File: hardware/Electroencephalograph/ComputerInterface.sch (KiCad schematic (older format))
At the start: 14 parts, among them J5 USB_B_Micro, U6 FT200XD

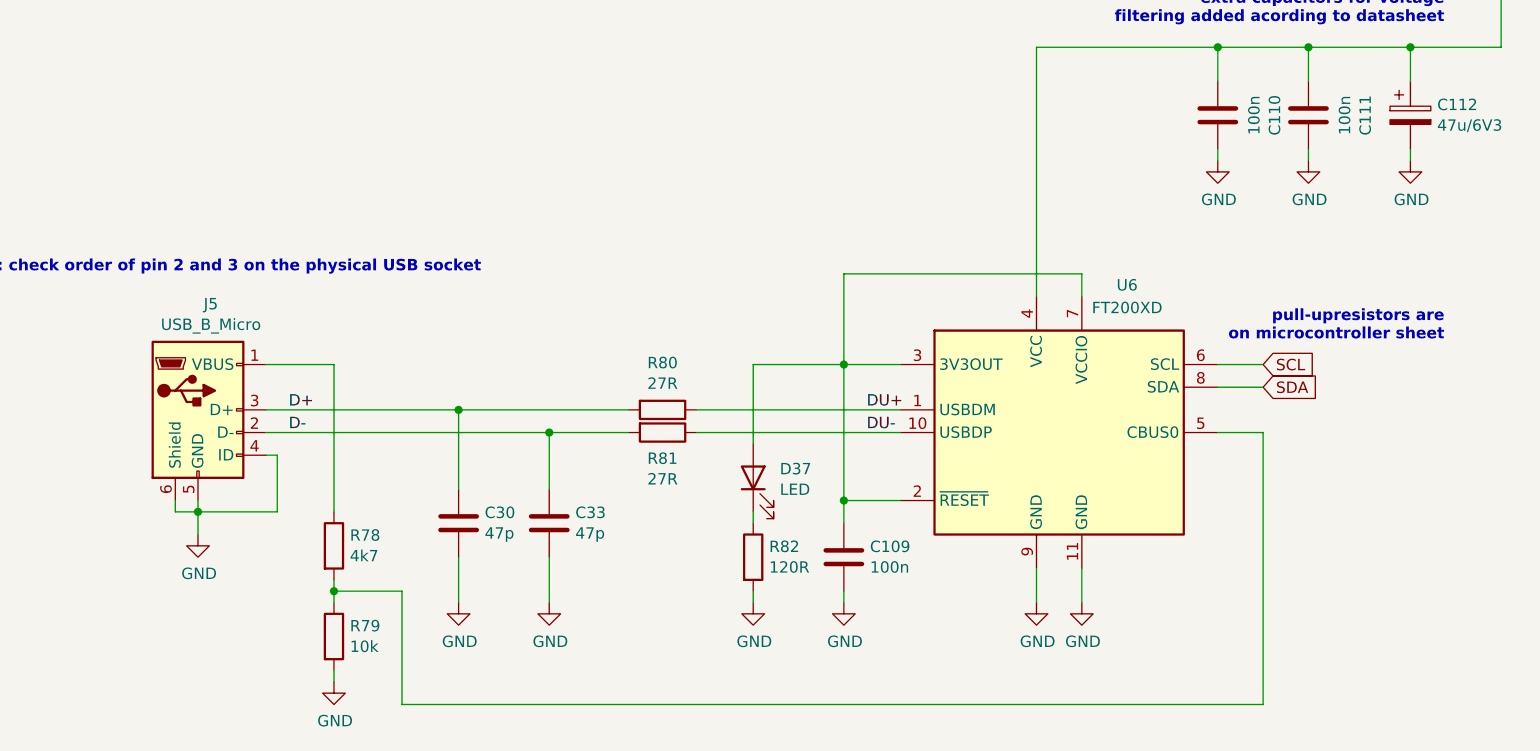
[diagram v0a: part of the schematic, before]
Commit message: placement of usb interface, fix in grounds
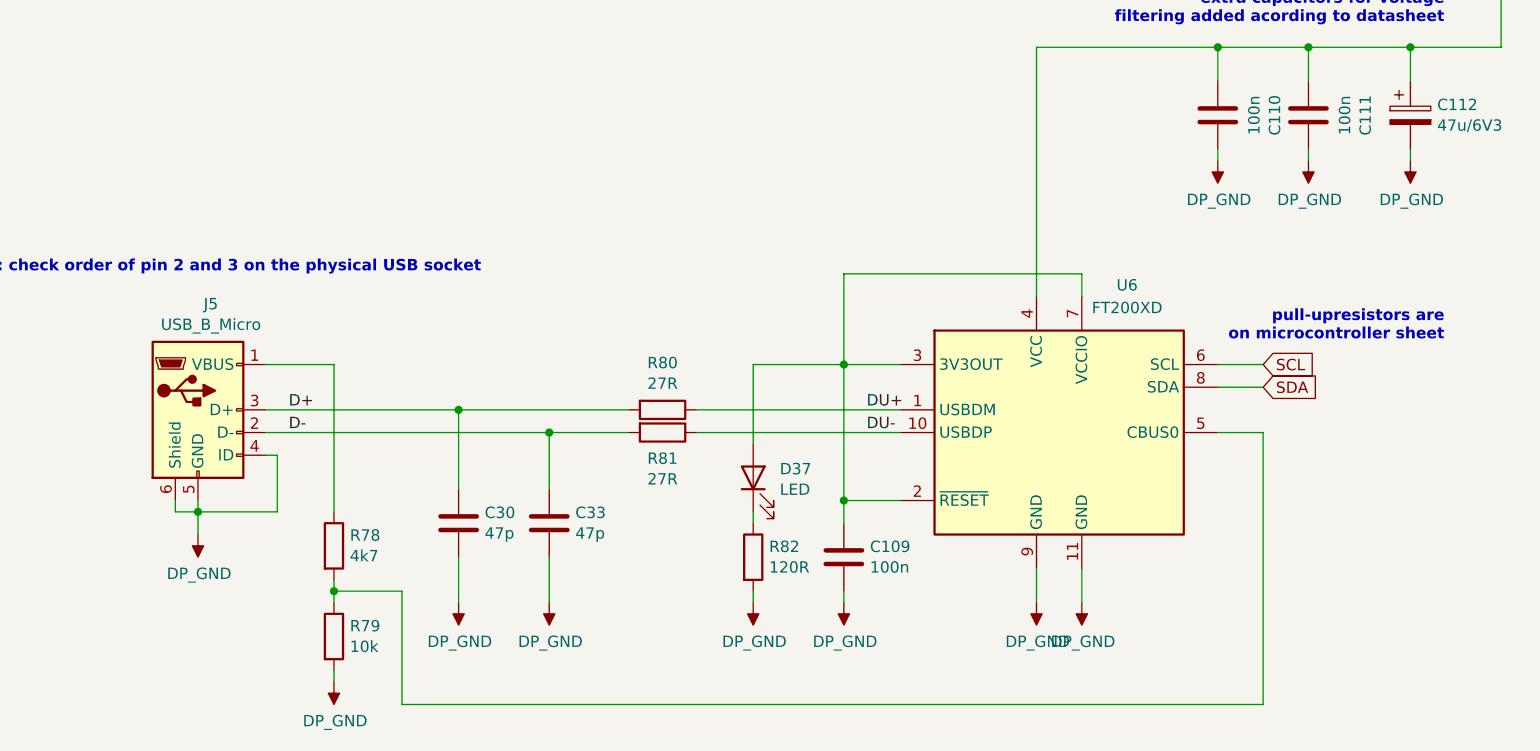
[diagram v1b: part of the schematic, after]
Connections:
- net GND renamed DP_GND
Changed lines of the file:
@@
 encoding utf-8
 Sheet 8 8
-Title ""
+Title "Computer interface"
 Date ""
-Rev ""
-Comp ""
+Rev "1.0"
+Comp "MIT License"
 Comment1 ""
 Comment2 ""
@@
 $EndComp
 $Comp
-L power:GND #PWR?
+L Electroencephalograph:DP_GND #PWR?
 U 1 1 5DDD73E7
 P 3250 4350
@@
 AR Path="/5E27E78E/5DDD73E7" Ref="#PWR057"  Part="1"
 F 0 "#PWR057" H 3250 4100 50  0001 C CNN
-F 1 "GND" H 3255 4177 50  0000 C CNN
+F 1 "DP_GND" H 3255 4177 50  0000 C CNN
 F 2 "" H 3250 4350 50  0001 C CNN
 F 3 "" H 3250 4350 50  0001 C CNN
@@
 	5700 4250 5700 4300
 $Comp
-L power:GND #PWR?
+L Electroencephalograph:DP_GND #PWR?
 U 1 1 5DDD73F8
 P 5700 4650
@@
 AR Path="/5E27E78E/5DDD73F8" Ref="#PWR0197"  Part="1"
 F 0 "#PWR0197" H 5700 4400 50  0001 C CNN
-F 1 "GND" H 5705 4477 50  0000 C CNN
+F 1 "DP_GND" H 5705 4477 50  0000 C CNN
 F 2 "" H 5700 4650 50  0001 C CNN
 F 3 "" H 5700 4650 50  0001 C CNN
@@
 	5700 4650 5700 4600
 $Comp
-L power:GND #PWR?
+L Electroencephalograph:DP_GND #PWR?
 U 1 1 5DD1D08B
 P 6950 4650
@@
 AR Path="/5E27E78E/5DD1D08B" Ref="#PWR0199"  Part="1"
 F 0 "#PWR0199" H 6950 4400 50  0001 C CNN
-F 1 "GND" H 6955 4477 50  0000 C CNN
+F 1 "DP_GND" H 6955 4477 50  0000 C CNN
 F 2 "" H 6950 4650 50  0001 C CNN
 F 3 "" H 6950 4650 50  0001 C CNN
@@
 $EndComp
 $Comp
-L power:GND #PWR?
+L Electroencephalograph:DP_GND #PWR?
 U 1 1 5DD1D475
 P 7150 4650
@@
 AR Path="/5E27E78E/5DD1D475" Ref="#PWR0200"  Part="1"
 F 0 "#PWR0200" H 7150 4400 50  0001 C CNN
-F 1 "GND" H 7155 4477 50  0000 C CNN
+F 1 "DP_GND" H 7155 4477 50  0000 C CNN
 F 2 "" H 7150 4650 50  0001 C CNN
 F 3 "" H 7150 4650 50  0001 C CNN
@@
 	4400 3800 4400 4150
 $Comp
-L power:GND #PWR?
+L Electroencephalograph:DP_GND #PWR?
 U 1 1 5DD256FC
 P 4400 4650
@@
 AR Path="/5E27E78E/5DD256FC" Ref="#PWR064"  Part="1"
 F 0 "#PWR064" H 4400 4400 50  0001 C CNN
-F 1 "GND" H 4405 4477 50  0000 C CNN
+F 1 "DP_GND" H 4405 4477 50  0000 C CNN
 F 2 "" H 4400 4650 50  0001 C CNN
 F 3 "" H 4400 4650 50  0001 C CNN
@@
 $EndComp
 $Comp
-L power:GND #PWR?
+L Electroencephalograph:DP_GND #PWR?
 U 1 1 5DD25C76
 P 4800 4650
@@
 AR Path="/5E27E78E/5DD25C76" Ref="#PWR0196"  Part="1"
 F 0 "#PWR0196" H 4800 4400 50  0001 C CNN
-F 1 "GND" H 4805 4477 50  0000 C CNN
+F 1 "DP_GND" H 4805 4477 50  0000 C CNN
 F 2 "" H 4800 4650 50  0001 C CNN
 F 3 "" H 4800 4650 50  0001 C CNN
@@
 $EndComp
 $Comp
-L power:GND #PWR?
+L Electroencephalograph:DP_GND #PWR?
 U 1 1 5DD2774B
 P 6100 4650
@@
 AR Path="/5E27E78E/5DD2774B" Ref="#PWR0198"  Part="1"
 F 0 "#PWR0198" H 6100 4400 50  0001 C CNN
-F 1 "GND" H 6105 4477 50  0000 C CNN
+F 1 "DP_GND" H 6105 4477 50  0000 C CNN
 F 2 "" H 6100 4650 50  0001 C CNN
 F 3 "" H 6100 4650 50  0001 C CNN
@@
 	3850 3600 3850 4250
 $Comp
-L power:GND #PWR?
+L Electroencephalograph:DP_GND #PWR?
 U 1 1 5DD46299
 P 3850 5000
@@
 AR Path="/5E27E78E/5DD46299" Ref="#PWR058"  Part="1"
 F 0 "#PWR058" H 3850 4750 50  0001 C CNN
-F 1 "GND" H 3855 4827 50  0000 C CNN
+F 1 "DP_GND" H 3855 4827 50  0000 C CNN
 F 2 "" H 3850 5000 50  0001 C CNN
 F 3 "" H 3850 5000 50  0001 C CNN
@@
 $EndComp
 $Comp
-L power:GND #PWR?
+L Electroencephalograph:DP_GND #PWR?
 U 1 1 5DE7AD55
 P 8600 2700
@@
 AR Path="/5E27E78E/5DE7AD55" Ref="#PWR0203"  Part="1"
 F 0 "#PWR0203" H 8600 2450 50  0001 C CNN
-F 1 "GND" H 8605 2527 50  0000 C CNN
+F 1 "DP_GND" H 8605 2527 50  0000 C CNN
 F 2 "" H 8600 2700 50  0001 C CNN
 F 3 "" H 8600 2700 50  0001 C CNN
@@
 $EndComp
 $Comp
-L power:GND #PWR?
+L Electroencephalograph:DP_GND #PWR?
 U 1 1 5DE8245F
 P 8150 2700
@@
 AR Path="/5E27E78E/5DE8245F" Ref="#PWR0202"  Part="1"
 F 0 "#PWR0202" H 8150 2450 50  0001 C CNN
-F 1 "GND" H 8155 2527 50  0000 C CNN
+F 1 "DP_GND" H 8155 2527 50  0000 C CNN
 F 2 "" H 8150 2700 50  0001 C CNN
 F 3 "" H 8150 2700 50  0001 C CNN
@@
 $EndComp
 $Comp
-L power:GND #PWR?
+L Electroencephalograph:DP_GND #PWR?
 U 1 1 5DE8272A
 P 7750 2700
@@
 AR Path="/5E27E78E/5DE8272A" Ref="#PWR0201"  Part="1"
 F 0 "#PWR0201" H 7750 2450 50  0001 C CNN
-F 1 "GND" H 7755 2527 50  0000 C CNN
+F 1 "DP_GND" H 7755 2527 50  0000 C CNN
 F 2 "" H 7750 2700 50  0001 C CNN
 F 3 "" H 7750 2700 50  0001 C CNN

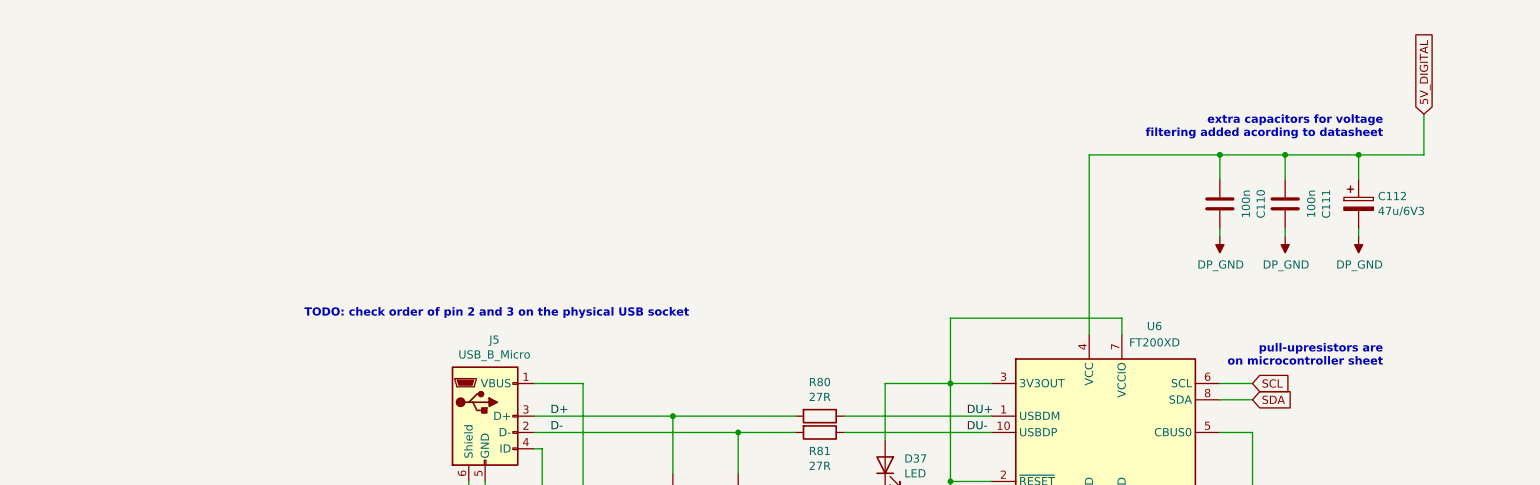
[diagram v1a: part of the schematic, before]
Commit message: fix #41, fix #18
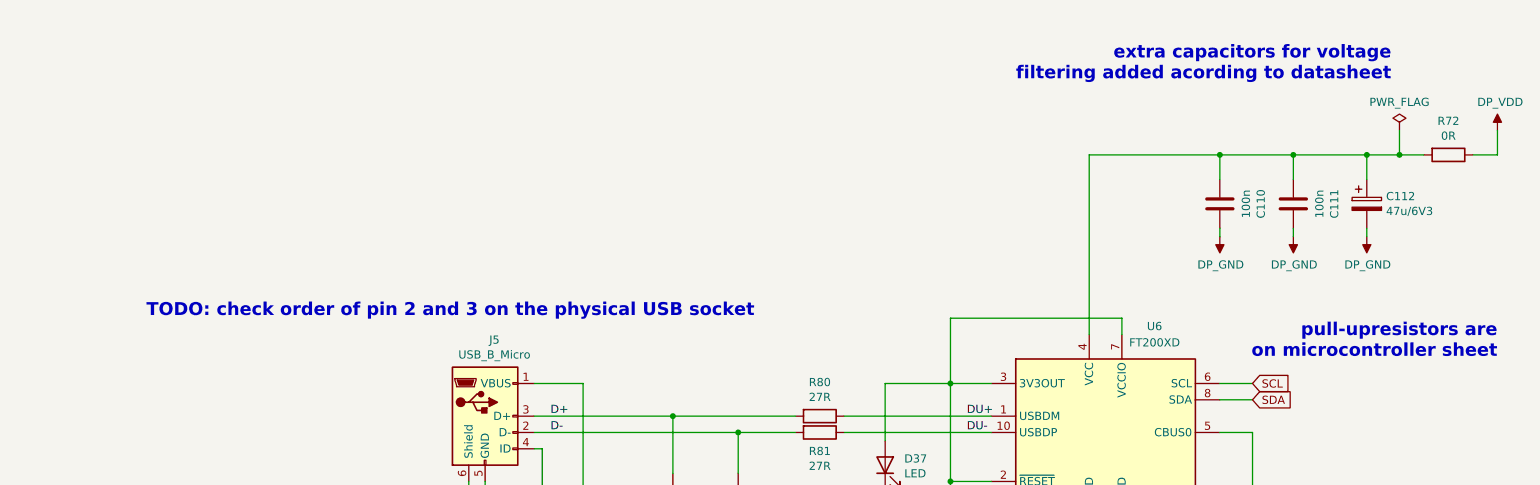
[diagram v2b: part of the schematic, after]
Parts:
- added R72: 0R, Resistor_SMD:R_0402_1005Metric, symbol Device:R
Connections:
- net 5V_DIGITAL: no longer names the net of C110.1, C111.1, C112.1, U6.4 (VCC)
- net 5V_DIGITAL: now also R72.2
- new net DP_VDD: R72.1
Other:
- moved on the sheet: C111, C112
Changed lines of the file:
@@
 $Descr A4 11693 8268
 encoding utf-8
-Sheet 8 8
+Sheet 8 9
 Title "Computer interface"
 Date ""
@@
 AR Path="/5DD5C7F6/5DDD73E7" Ref="#PWR?"  Part="1"
 AR Path="/5DD5CD1D/5DDD73E7" Ref="#PWR?"  Part="1"
-AR Path="/5E27E78E/5DDD73E7" Ref="#PWR057"  Part="1"
-F 0 "#PWR057" H 3250 4100 50  0001 C CNN
+AR Path="/5E27E78E/5DDD73E7" Ref="#PWR57"  Part="1"
+F 0 "#PWR57" H 3250 4100 50  0001 C CNN
 F 1 "DP_GND" H 3255 4177 50  0000 C CNN
 F 2 "" H 3250 4350 50  0001 C CNN
@@
 AR Path="/5DD5C7F6/5DDD73F8" Ref="#PWR?"  Part="1"
 AR Path="/5DD5CD1D/5DDD73F8" Ref="#PWR?"  Part="1"
-AR Path="/5E27E78E/5DDD73F8" Ref="#PWR0197"  Part="1"
-F 0 "#PWR0197" H 5700 4400 50  0001 C CNN
+AR Path="/5E27E78E/5DDD73F8" Ref="#PWR197"  Part="1"
+F 0 "#PWR197" H 5700 4400 50  0001 C CNN
 F 1 "DP_GND" H 5705 4477 50  0000 C CNN
 F 2 "" H 5700 4650 50  0001 C CNN
@@
 AR Path="/5DD5C7F6/5DD1D08B" Ref="#PWR?"  Part="1"
 AR Path="/5DD5CD1D/5DD1D08B" Ref="#PWR?"  Part="1"
-AR Path="/5E27E78E/5DD1D08B" Ref="#PWR0199"  Part="1"
-F 0 "#PWR0199" H 6950 4400 50  0001 C CNN
+AR Path="/5E27E78E/5DD1D08B" Ref="#PWR199"  Part="1"
+F 0 "#PWR199" H 6950 4400 50  0001 C CNN
 F 1 "DP_GND" H 6955 4477 50  0000 C CNN
 F 2 "" H 6950 4650 50  0001 C CNN
@@
 AR Path="/5DD5C7F6/5DD1D475" Ref="#PWR?"  Part="1"
 AR Path="/5DD5CD1D/5DD1D475" Ref="#PWR?"  Part="1"
-AR Path="/5E27E78E/5DD1D475" Ref="#PWR0200"  Part="1"
-F 0 "#PWR0200" H 7150 4400 50  0001 C CNN
+AR Path="/5E27E78E/5DD1D475" Ref="#PWR200"  Part="1"
+F 0 "#PWR200" H 7150 4400 50  0001 C CNN
 F 1 "DP_GND" H 7155 4477 50  0000 C CNN
 F 2 "" H 7150 4650 50  0001 C CNN
@@
 Text GLabel 7950 3700 2    50   Input ~ 0
 SDA
-Text Notes 8750 3500 2    50   ~ 10
+Text Notes 9450 3450 2    79   ~ 16
 pull-upresistors are \non microcontroller sheet
 Wire Wire Line
@@
 AR Path="/5DD5C7F6/5DD256FC" Ref="#PWR?"  Part="1"
 AR Path="/5DD5CD1D/5DD256FC" Ref="#PWR?"  Part="1"
-AR Path="/5E27E78E/5DD256FC" Ref="#PWR064"  Part="1"
-F 0 "#PWR064" H 4400 4400 50  0001 C CNN
+AR Path="/5E27E78E/5DD256FC" Ref="#PWR64"  Part="1"
+F 0 "#PWR64" H 4400 4400 50  0001 C CNN
 F 1 "DP_GND" H 4405 4477 50  0000 C CNN
 F 2 "" H 4400 4650 50  0001 C CNN
@@
 AR Path="/5DD5C7F6/5DD25C76" Ref="#PWR?"  Part="1"
 AR Path="/5DD5CD1D/5DD25C76" Ref="#PWR?"  Part="1"
-AR Path="/5E27E78E/5DD25C76" Ref="#PWR0196"  Part="1"
-F 0 "#PWR0196" H 4800 4400 50  0001 C CNN
+AR Path="/5E27E78E/5DD25C76" Ref="#PWR196"  Part="1"
+F 0 "#PWR196" H 4800 4400 50  0001 C CNN
 F 1 "DP_GND" H 4805 4477 50  0000 C CNN
 F 2 "" H 4800 4650 50  0001 C CNN
@@
 AR Path="/5DD5C7F6/5DD2774B" Ref="#PWR?"  Part="1"
 AR Path="/5DD5CD1D/5DD2774B" Ref="#PWR?"  Part="1"
-AR Path="/5E27E78E/5DD2774B" Ref="#PWR0198"  Part="1"
-F 0 "#PWR0198" H 6100 4400 50  0001 C CNN
+AR Path="/5E27E78E/5DD2774B" Ref="#PWR198"  Part="1"
+F 0 "#PWR198" H 6100 4400 50  0001 C CNN
 F 1 "DP_GND" H 6105 4477 50  0000 C CNN
 F 2 "" H 6100 4650 50  0001 C CNN
@@
 Wire Wire Line
 	3600 4250 3250 4250
-Text Notes 4500 3200 2    50   ~ 10
+Text Notes 4900 3200 2    79   ~ 16
 TODO: check order of pin 2 and 3 on the physical USB socket
 Wire Wire Line
@@
 	6100 3200 6100 3600
 Wire Wire Line
-	9000 1950 9000 2200
+	9450 2050 9450 2200
 $Comp
 L Device:C C?
@@
 AR Path="/5DD5C7F6/5DD46299" Ref="#PWR?"  Part="1"
 AR Path="/5DD5CD1D/5DD46299" Ref="#PWR?"  Part="1"
-AR Path="/5E27E78E/5DD46299" Ref="#PWR058"  Part="1"
-F 0 "#PWR058" H 3850 4750 50  0001 C CNN
+AR Path="/5E27E78E/5DD46299" Ref="#PWR58"  Part="1"
+F 0 "#PWR58" H 3850 4750 50  0001 C CNN
 F 1 "DP_GND" H 3855 4827 50  0000 C CNN
 F 2 "" H 3850 5000 50  0001 C CNN
@@
 Wire Wire Line
 	5450 3800 6350 3800
-Text GLabel 9000 1950 1    50   Input ~ 0
-5V_DIGITAL
 Wire Wire Line
 	6100 3600 5700 3600
@@
 L Device:CP C?
 U 1 1 5DE7AD4F
-P 8600 2500
+P 8650 2500
 AR Path="/5DE7AD4F" Ref="C?"  Part="1"
 AR Path="/5DAEEEF4/5DE7AD4F" Ref="C?"  Part="1"
@@
 AR Path="/5DD5CD1D/5DE7AD4F" Ref="C?"  Part="1"
 AR Path="/5E27E78E/5DE7AD4F" Ref="C112"  Part="1"
-F 0 "C112" H 8718 2546 50  0000 L CNN
-F 1 "47u/6V3" H 8718 2455 50  0000 L CNN
-F 2 "Capacitor_Tantalum_SMD:CP_EIA-3528-21_Kemet-B" H 8638 2350 50  0001 C CNN
-F 3 "~" H 8600 2500 50  0001 C CNN
-	1    8600 2500
+F 0 "C112" H 8768 2546 50  0000 L CNN
+F 1 "47u/6V3" H 8768 2455 50  0000 L CNN
+F 2 "Capacitor_Tantalum_SMD:CP_EIA-3528-21_Kemet-B" H 8688 2350 50  0001 C CNN
+F 3 "~" H 8650 2500 50  0001 C CNN
+	1    8650 2500
 	1    0    0    -1
 $EndComp
@@
 L Electroencephalograph:DP_GND #PWR?
 U 1 1 5DE7AD55
-P 8600 2700
+P 8650 2700
 AR Path="/5DE7AD55" Ref="#PWR?"  Part="1"
 AR Path="/5DAEEEF4/5DE7AD55" Ref="#PWR?"  Part="1"
 AR Path="/5DD5C7F6/5DE7AD55" Ref="#PWR?"  Part="1"
 AR Path="/5DD5CD1D/5DE7AD55" Ref="#PWR?"  Part="1"
-AR Path="/5E27E78E/5DE7AD55" Ref="#PWR0203"  Part="1"
-F 0 "#PWR0203" H 8600 2450 50  0001 C CNN
-F 1 "DP_GND" H 8605 2527 50  0000 C CNN
-F 2 "" H 8600 2700 50  0001 C CNN
-F 3 "" H 8600 2700 50  0001 C CNN
-	1    8600 2700
-	1    0    0    -1
-$EndComp
-Wire Wire Line
-	8600 2700 8600 2650
+AR Path="/5E27E78E/5DE7AD55" Ref="#PWR203"  Part="1"
+F 0 "#PWR203" H 8650 2450 50  0001 C CNN
+F 1 "DP_GND" H 8655 2527 50  0000 C CNN
+F 2 "" H 8650 2700 50  0001 C CNN
+F 3 "" H 8650 2700 50  0001 C CNN
+	1    8650 2700
+	1    0    0    -1
+$EndComp
+Wire Wire Line
+	8650 2700 8650 2650
 $Comp
 L Device:C C?
 U 1 1 5DE7B775
-P 8150 2500
+P 8200 2500
 AR Path="/5DE7B775" Ref="C?"  Part="1"
 AR Path="/5DAEEEF4/5DE7B775" Ref="C?"  Part="1"
@@
 AR Path="/5DD5CD1D/5DE7B775" Ref="C?"  Part="1"
 AR Path="/5E27E78E/5DE7B775" Ref="C111"  Part="1"
-F 0 "C111" V 8402 2500 50  0000 C CNN
-F 1 "100n" V 8311 2500 50  0000 C CNN
-F 2 "Capacitor_SMD:C_0402_1005Metric" H 8188 2350 50  0001 C CNN
-F 3 "~" H 8150 2500 50  0001 C CNN
-	1    8150 2500
+F 0 "C111" V 8452 2500 50  0000 C CNN
+F 1 "100n" V 8361 2500 50  0000 C CNN
+F 2 "Capacitor_SMD:C_0402_1005Metric" H 8238 2350 50  0001 C CNN
+F 3 "~" H 8200 2500 50  0001 C CNN
+	1    8200 2500
 	1    0    0    -1
 $EndComp
@@
 L Electroencephalograph:DP_GND #PWR?
 U 1 1 5DE8245F
-P 8150 2700
+P 8200 2700
 AR Path="/5DE8245F" Ref="#PWR?"  Part="1"
 AR Path="/5DAEEEF4/5DE8245F" Ref="#PWR?"  Part="1"
 AR Path="/5DD5C7F6/5DE8245F" Ref="#PWR?"  Part="1"
 AR Path="/5DD5CD1D/5DE8245F" Ref="#PWR?"  Part="1"
-AR Path="/5E27E78E/5DE8245F" Ref="#PWR0202"  Part="1"
-F 0 "#PWR0202" H 8150 2450 50  0001 C CNN
-F 1 "DP_GND" H 8155 2527 50  0000 C CNN
-F 2 "" H 8150 2700 50  0001 C CNN
-F 3 "" H 8150 2700 50  0001 C CNN
-	1    8150 2700
+AR Path="/5E27E78E/5DE8245F" Ref="#PWR202"  Part="1"
+F 0 "#PWR202" H 8200 2450 50  0001 C CNN
+F 1 "DP_GND" H 8205 2527 50  0000 C CNN
+F 2 "" H 8200 2700 50  0001 C CNN
+F 3 "" H 8200 2700 50  0001 C CNN
+	1    8200 2700
 	1    0    0    -1
 $EndComp
@@
 AR Path="/5DD5C7F6/5DE8272A" Ref="#PWR?"  Part="1"
 AR Path="/5DD5CD1D/5DE8272A" Ref="#PWR?"  Part="1"
-AR Path="/5E27E78E/5DE8272A" Ref="#PWR0201"  Part="1"
-F 0 "#PWR0201" H 7750 2450 50  0001 C CNN
+AR Path="/5E27E78E/5DE8272A" Ref="#PWR201"  Part="1"
+F 0 "#PWR201" H 7750 2450 50  0001 C CNN
 F 1 "DP_GND" H 7755 2527 50  0000 C CNN
 F 2 "" H 7750 2700 50  0001 C CNN
@@
 	7750 2700 7750 2650
 Wire Wire Line
-	8150 2700 8150 2650
-Wire Wire Line
-	9000 2200 8600 2200
+	8200 2700 8200 2650
 Wire Wire Line
 	7750 2200 7750 2350
 Wire Wire Line
-	8150 2350 8150 2200
-Connection ~ 8150 2200
-Wire Wire Line
-	8150 2200 7750 2200
-Wire Wire Line
-	8600 2350 8600 2200
-Connection ~ 8600 2200
-Wire Wire Line
-	8600 2200 8150 2200
-Text Notes 8750 2100 2    50   ~ 10
+	8200 2350 8200 2200
+Wire Wire Line
+	8650 2350 8650 2200
+Text Notes 8800 1750 2    79   ~ 16
 extra capacitors for voltage\nfiltering added acording to datasheet\n
 Wire Wire Line
 	7750 2200 6950 2200
-Connection ~ 7750 2200
 Wire Wire Line
 	6950 2200 6950 3300
@@
 Text Label 6200 3900 0    50   ~ 0
 DU-
+$Comp
+L Electroencephalograph:DP_VDD #PWR212
+U 1 1 5EC92542
+P 9450 2050
+F 0 "#PWR212" H 9450 2175 50  0001 C CNN
+F 1 "DP_VDD" H 9467 2223 50  0000 C CNN
+F 2 "" H 9450 2175 50  0001 C CNN
+F 3 "" H 9450 2175 50  0001 C CNN
+	1    9450 2050
+	1    0    0    -1
+$EndComp
+Connection ~ 7750 2200
+Wire Wire Line
+	7750 2200 8200 2200
+Wire Wire Line
+	8200 2200 8650 2200
+Connection ~ 8200 2200
+$Comp
+L Device:R R?
+U 1 1 5ED1AA8A
+P 9150 2200
+AR Path="/5DD5C7F6/5ED1AA8A" Ref="R?"  Part="1"
+AR Path="/5DD5CD1D/5ED1AA8A" Ref="R?"  Part="1"
+AR Path="/5E27E78E/5ED1AA8A" Ref="R72"  Part="1"
+F 0 "R72" V 8943 2200 50  0000 C CNN
+F 1 "0R" V 9034 2200 50  0000 C CNN
+F 2 "Resistor_SMD:R_0402_1005Metric" V 9080 2200 50  0001 C CNN
+F 3 "~" H 9150 2200 50  0001 C CNN
+	1    9150 2200
+	0    1    1    0
+$EndComp
+Wire Wire Line
+	8650 2200 8850 2200
+Connection ~ 8650 2200
+Wire Wire Line
+	9300 2200 9450 2200
+$Comp
+L power:PWR_FLAG #FLG02
+U 1 1 5ED1FF8B
+P 8850 2050
+F 0 "#FLG02" H 8850 2125 50  0001 C CNN
+F 1 "PWR_FLAG" H 8850 2223 50  0000 C CNN
+F 2 "" H 8850 2050 50  0001 C CNN
+F 3 "~" H 8850 2050 50  0001 C CNN
+	1    8850 2050
+	1    0    0    -1
+$EndComp
+Wire Wire Line
+	8850 2050 8850 2200
+Connection ~ 8850 2200
+Wire Wire Line
+	8850 2200 9000 2200
 $EndSCHEMATC
